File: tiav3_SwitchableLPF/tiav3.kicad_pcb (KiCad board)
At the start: 4 copper layers, 25.3 x 25.3 mm, 37 parts, among them J1 SSQ-103-01-G-D, J2 Conn_Coaxial, J3 SSQ-102-01-G-D, U1 OPA847IDBVT, U2 OPA842xDBV, U3 TMUX1209RSVR

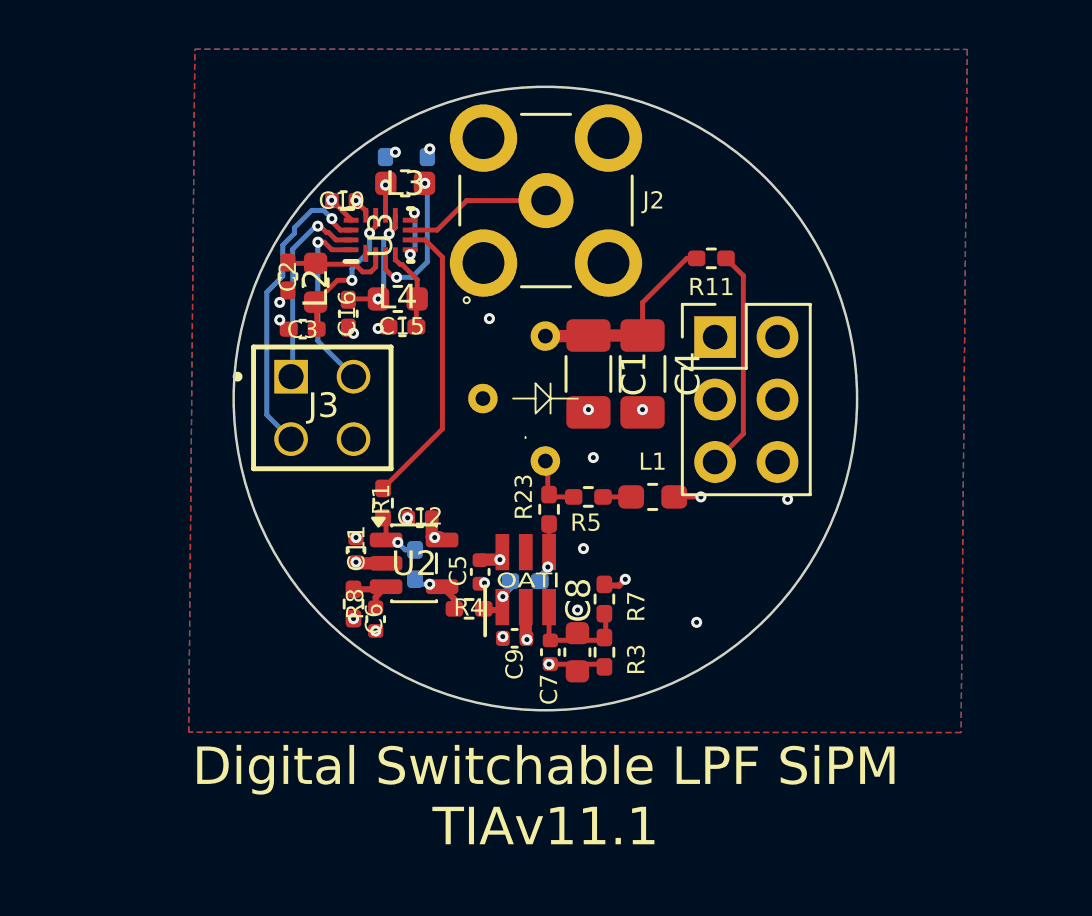
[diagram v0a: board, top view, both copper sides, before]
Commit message: Performed claude analysis on the project and fixed risk 4
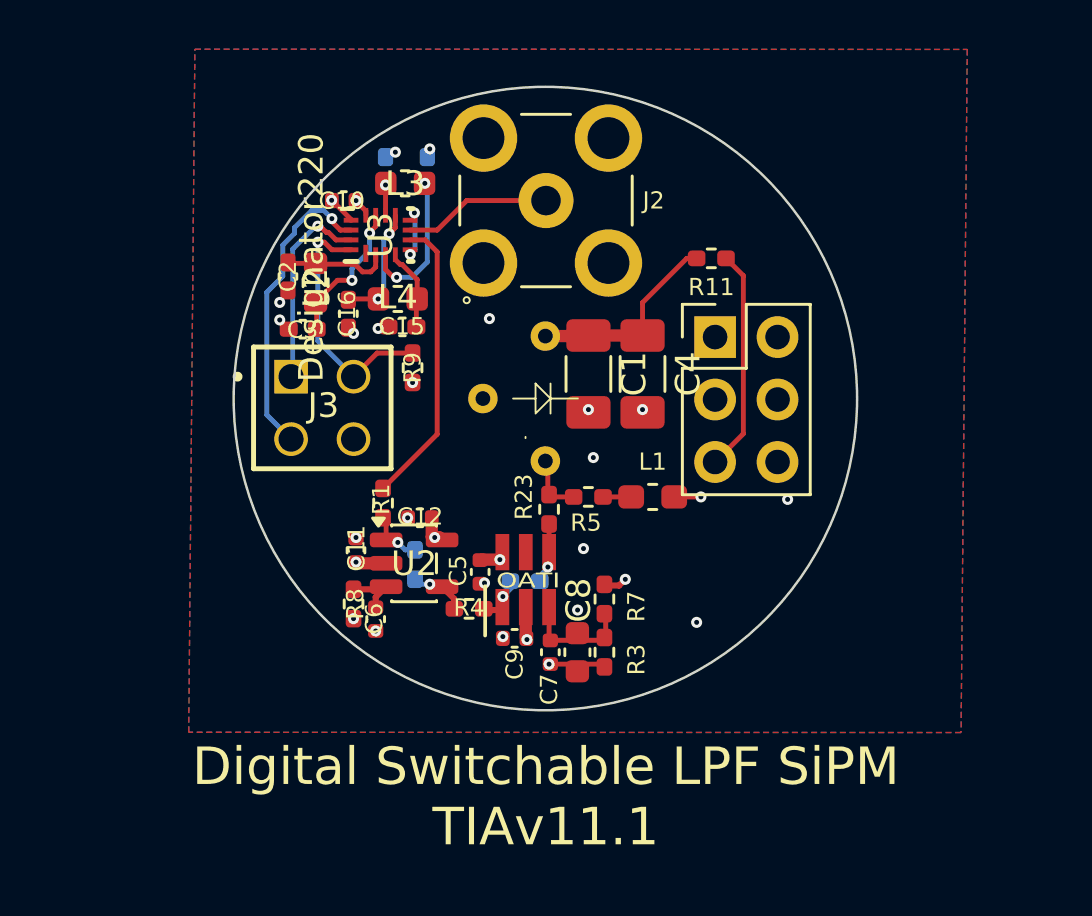
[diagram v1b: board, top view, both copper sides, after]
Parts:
- added R9: 10k, Resistor_SMD:R_0402_1005Metric_Pad0.72x0.64mm_HandSolder, F.Cu at (194.6, 98.7)
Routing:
- net EN: track 7.55 -> 10.3 mm
- net GND: vias 22 -> 23
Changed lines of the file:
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@@
 			(layer "F.Fab")
 		)
+		(fp_text user "Designator220"
+			(at -0.914395 -2.81941 90)
+			(unlocked yes)
+			(layer "F.SilkS")
+			(effects
+				(font
+					(size 1 1)
+					(thickness 0.15)
+				)
+			)
+		)
 		(fp_text user "${REFERENCE}"
 			(at 0 0 90)
@@
 		)
 	)
+	(footprint "Resistor_SMD:R_0402_1005Metric_Pad0.72x0.64mm_HandSolder"
+		(layer "F.Cu")
+		(at 194.6 98.7475 90)
+		(descr "Resistor SMD 0402 (1005 Metric), square (rectangular) end terminal, IPC-7351 nominal with elongated pad for handsoldering. (Body size source: IPC-SM-782 page 72, https://www.pcb-3d.com/wordpress/wp-content/uploads/ipc-sm-782a_amendment_1_and_2.pdf), generated with kicad-footprint-generator")
+		(tags "resistor handsolder")
+		(property "Reference" "R9"
+			(at -0.0025 0 90)
+			(layer "F.SilkS")
+			(effects
+				(font
+					(size 0.7 0.7)
+					(thickness 0.15)
+				)
+			)
+		)
+		(property "Value" "10k"
+			(at 0 1.17 90)
+			(layer "F.Fab")
+			(effects
+				(font
+					(size 1 1)
+					(thickness 0.15)
+				)
+			)
+		)
+		(property "Datasheet" "~"
+			(at 0 0 90)
+			(layer "F.Fab")
+			(hide yes)
+			(effects
+				(font
+					(size 1.27 1.27)
+					(thickness 0.15)
+				)
+			)
+		)
+		(property "Description" ""
+			(at 0 0 90)
+			(layer "F.Fab")
+			(hide yes)
+			(effects
+				(font
+					(size 1.27 1.27)
+					(thickness 0.15)
+				)
+			)
+		)
+		(property ki_fp_filters "R_*")
+		(sheetname "/")
+		(sheetfile "tiav3.kicad_sch")
+		(attr smd)
+		(fp_line
+			(start -0.167621 -0.38)
+			(end 0.167621 -0.38)
+			(stroke
+				(width 0.12)
+				(type solid)
+			)
+			(layer "F.SilkS")
+		)
+		(fp_line
+			(start -0.167621 0.38)
+			(end 0.167621 0.38)
+			(stroke
+				(width 0.12)
+				(type solid)
+			)
+			(layer "F.SilkS")
+		)
+		(fp_line
+			(start 1.11 -0.47)
+			(end 1.11 0.47)
+			(stroke
+				(width 0.05)
+				(type solid)
+			)
+			(layer "F.CrtYd")
+		)
+		(fp_line
+			(start -1.11 -0.47)
+			(end 1.11 -0.47)
+			(stroke
+				(width 0.05)
+				(type solid)
+			)
+			(layer "F.CrtYd")
+		)
+		(fp_line
+			(start 1.11 0.47)
+			(end -1.11 0.47)
+			(stroke
+				(width 0.05)
+				(type solid)
+			)
+			(layer "F.CrtYd")
+		)
+		(fp_line
+			(start -1.11 0.47)
+			(end -1.11 -0.47)
+			(stroke
+				(width 0.05)
+				(type solid)
+			)
+			(layer "F.CrtYd")
+		)
+		(fp_line
+			(start 0.525 -0.27)
+			(end 0.525 0.27)
+			(stroke
+				(width 0.1)
+				(type solid)
+			)
+			(layer "F.Fab")
+		)
+		(fp_line
+			(start -0.525 -0.27)
+			(end 0.525 -0.27)
+			(stroke
+				(width 0.1)
+				(type solid)
+			)
+			(layer "F.Fab")
+		)
+		(fp_line
+			(start 0.525 0.27)
+			(end -0.525 0.27)
+			(stroke
+				(width 0.1)
+				(type solid)
+			)
+			(layer "F.Fab")
+		)
+		(fp_line
+			(start -0.525 0.27)
+			(end -0.525 -0.27)
+			(stroke
+				(width 0.1)
+				(type solid)
+			)
+			(layer "F.Fab")
+		)
+		(fp_text user "${REFERENCE}"
+			(at 0 0 90)
+			(layer "F.Fab")
+			(effects
+				(font
+					(size 0.26 0.26)
+					(thickness 0.04)
+				)
+			)
+		)
+		(pad "1" smd roundrect
+			(at -0.5975 0 90)
+			(size 0.715 0.64)
+			(layers "F.Cu" "F.Mask" "F.Paste")
+			(roundrect_rratio 0.25)
+			(net 1 "GND")
+			(pintype "passive")
+		)
+		(pad "2" smd roundrect
+			(at 0.5975 0 90)
+			(size 0.715 0.64)
+			(layers "F.Cu" "F.Mask" "F.Paste")
+			(roundrect_rratio 0.25)
+			(net 26 "EN")
+			(pintype "passive")
+		)
+		(embedded_fonts no)
+		(model "${KICAD9_3DMODEL_DIR}/Resistor_SMD.3dshapes/R_0402_1005Metric.step"
+			(offset
+				(xyz 0 0 0)
+			)
+			(scale
+				(xyz 1 1 1)
+			)
+			(rotate
+				(xyz 0 0 0)
+			)
+		)
+	)
 	(footprint "Capacitor_SMD:C_0402_1005Metric"
 		(layer "F.Cu")
@@
 	)
 	(via
+		(at 194.6 99.35)
+		(size 0.45)
+		(drill 0.2)
+		(layers "F.Cu" "B.Cu")
+		(net 1)
+	)
+	(via
 		(at 206.325 104)
 		(size 0.45)
@@
 	)
 	(segment
-		(start 193.4 103.6525)
-		(end 195.814 101.2385)
+		(start 195.114001 93.550001)
+		(end 194.500001 93.550001)
 		(width 0.2)
 		(layer "F.Cu")
@@
 	)
 	(segment
-		(start 195.114001 93.550001)
-		(end 194.500001 93.550001)
+		(start 193.4 103.6525)
+		(end 195.6 101.4525)
 		(width 0.2)
 		(layer "F.Cu")
@@
 	)
 	(segment
-		(start 195.814 101.2385)
-		(end 195.814 94.25)
+		(start 195.6 94.036)
+		(end 195.114001 93.550001)
 		(width 0.2)
 		(layer "F.Cu")
@@
 	)
 	(segment
-		(start 195.114001 93.550001)
-		(end 195.814 94.25)
+		(start 195.6 101.4525)
+		(end 195.6 94.036)
 		(width 0.2)
 		(layer "F.Cu")
@@
 	)
 	(segment
+		(start 192.2 99.11)
+		(end 193.16 98.15)
+		(width 0.2)
+		(layer "F.Cu")
+		(net 26)
+	)
+	(segment
 		(start 192.100001 93.95)
 		(end 191.31985 93.95)
@@
 		(net 26)
 	)
+	(segment
+		(start 193.16 98.15)
+		(end 194.6 98.15)
+		(width 0.2)
+		(layer "F.Cu")
+		(net 26)
+	)
 	(via
 		(at 190.75082 93.641644)
@@
 		(min_thickness 0.2)
 		(filled_areas_thickness no)
-		(fill yes
+		(fill
 			(thermal_gap 0.25)
 			(thermal_bridge_width 0.25)
@@
 		(min_thickness 0.25)
 		(filled_areas_thickness no)
-		(fill yes
+		(fill
 			(thermal_gap 0.5)
 			(thermal_bridge_width 0.5)
@@
 		(min_thickness 0.25)
 		(filled_areas_thickness no)
-		(fill yes
+		(fill
 			(thermal_gap 0.5)
 			(thermal_bridge_width 0.5)

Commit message: Created the 50 ohm impedance and changed EN pin to Ground
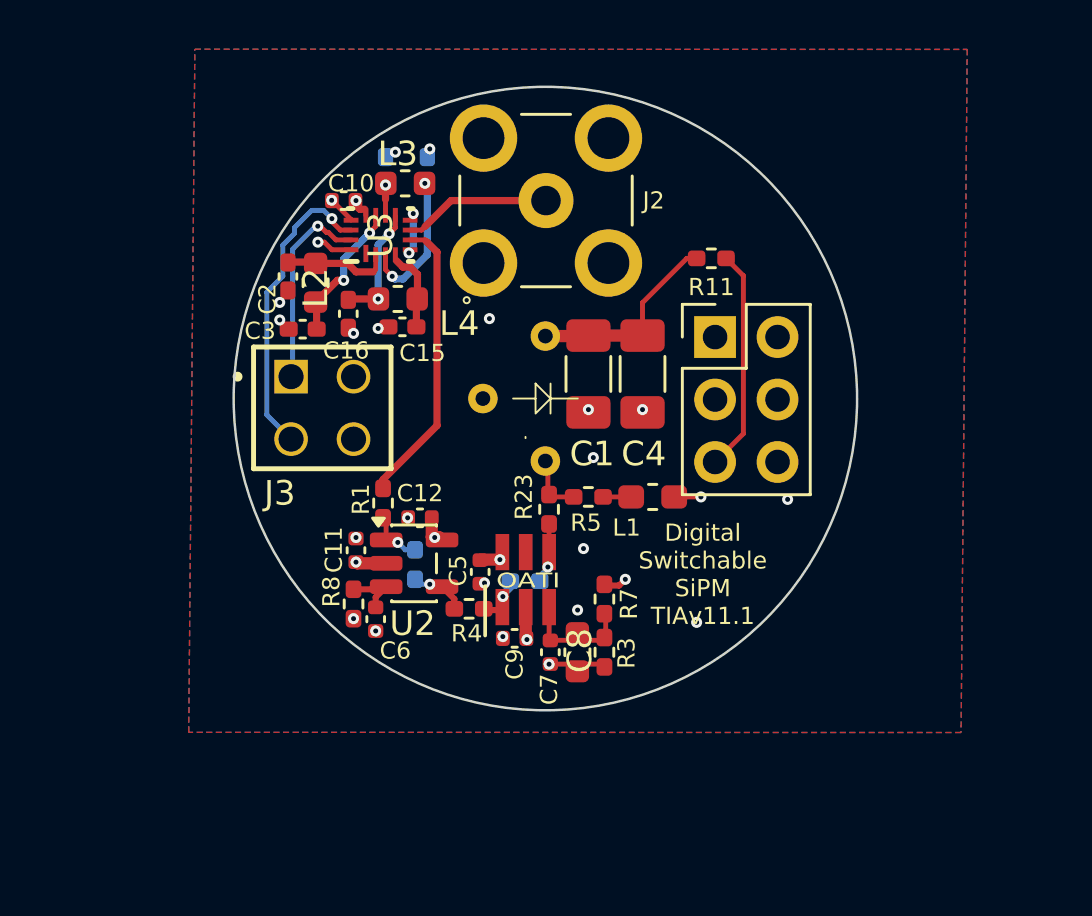
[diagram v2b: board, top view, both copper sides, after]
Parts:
- removed R9: 10k, Resistor_SMD:R_0402_1005Metric_Pad0.72x0.64mm_HandSolder
- R1: value 50 -> 45
- R8: value 400 -> 100
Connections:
- J3 pad 03: EN -> GND
- U3 pad 16: EN -> VDDA
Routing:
- net EN: track 10.3 -> 0.00 mm, vias 1 -> 0
- net VDDA: track 2.73 -> 4.24 mm, vias 3 -> 4
- net GND: vias 23 -> 22
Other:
- board text added: "Digital Switchable SiPM TIAv11.1"
- board text removed: "Digital Switchable LPF SiPM TIAv11.1"
